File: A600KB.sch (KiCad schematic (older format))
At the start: 84 parts

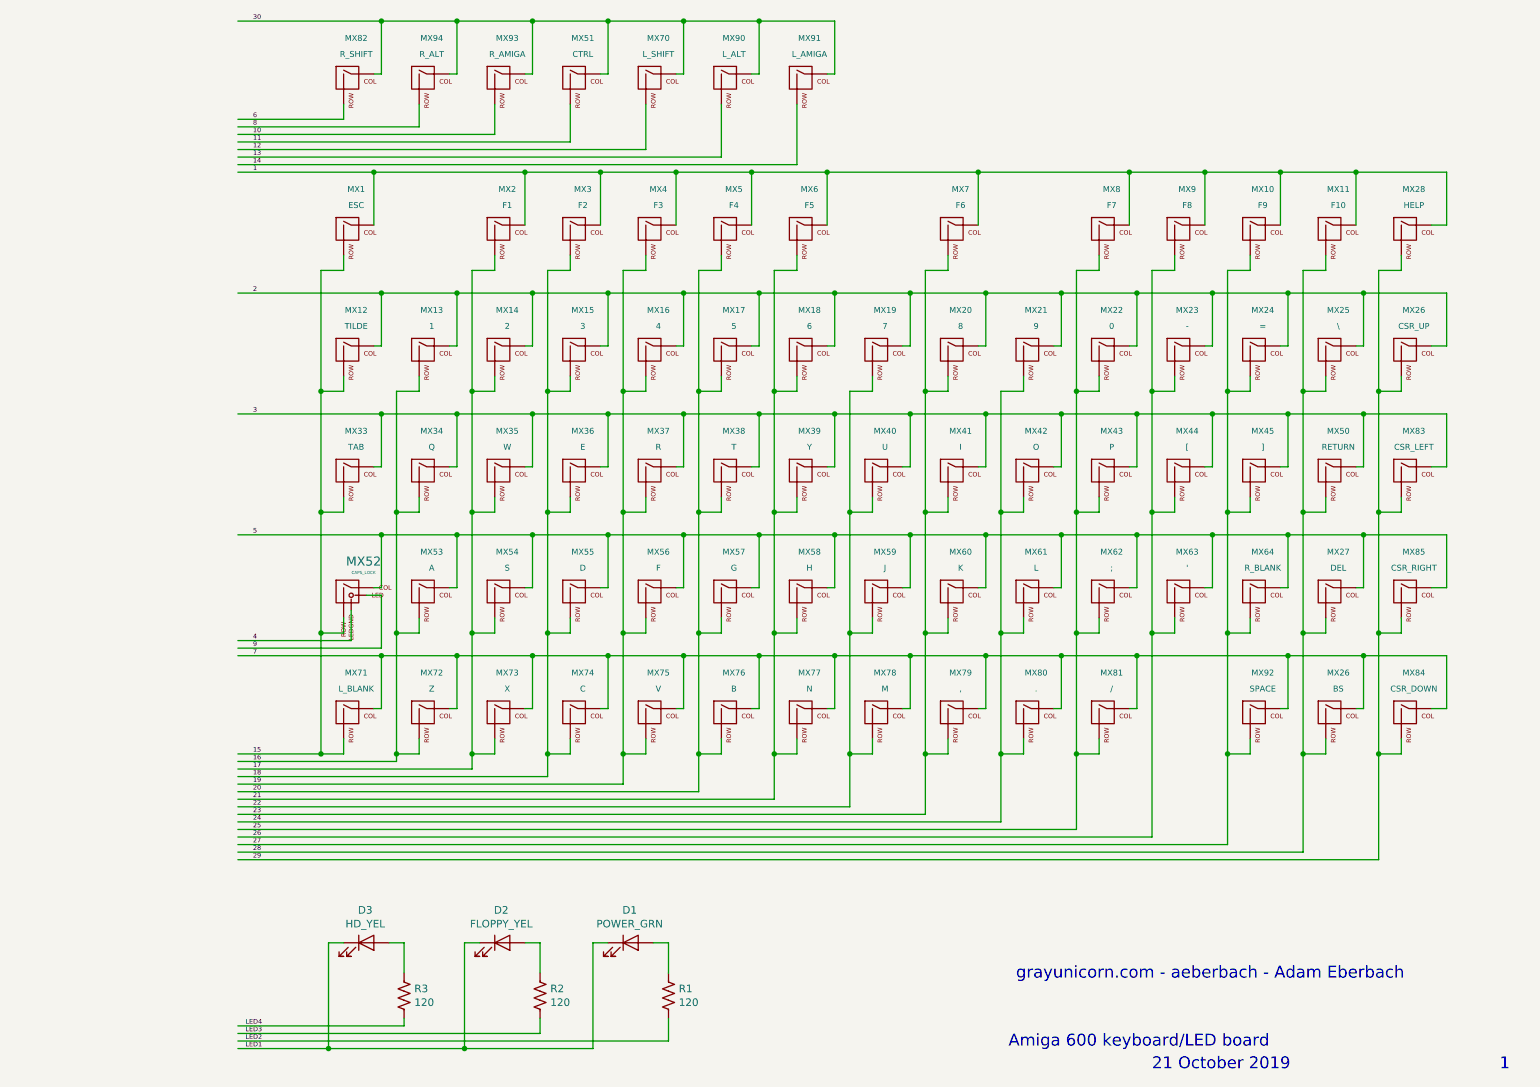
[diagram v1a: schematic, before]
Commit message: footprints for connectors
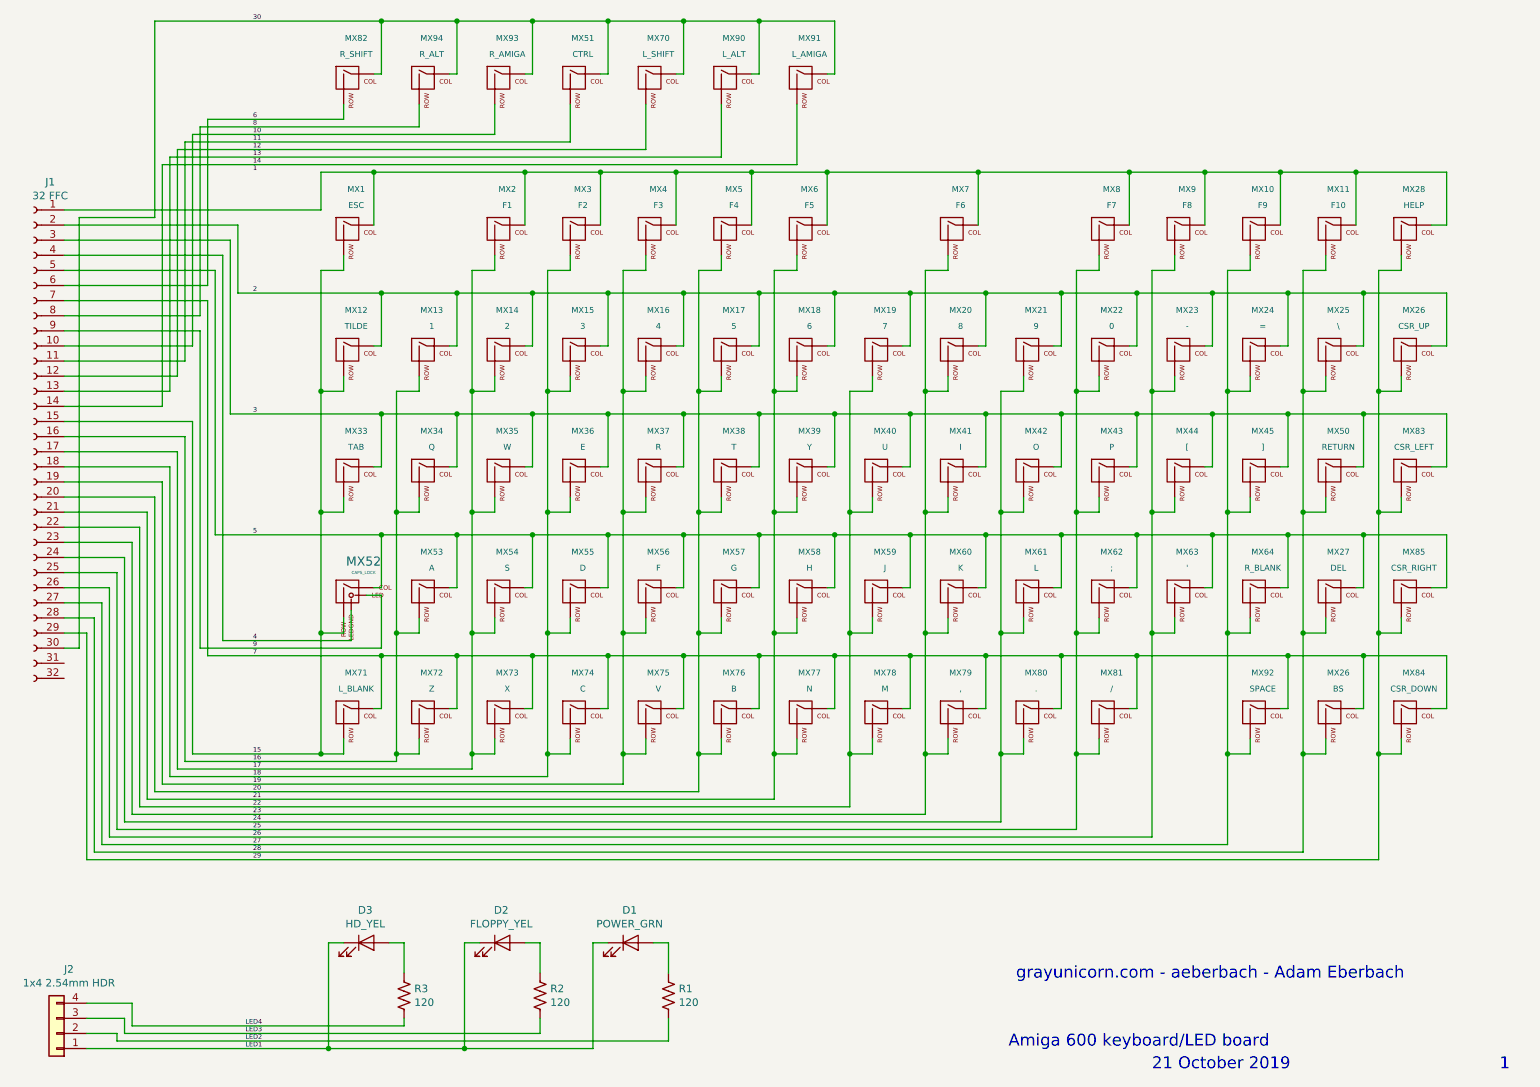
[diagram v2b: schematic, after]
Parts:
- added J1: 32 FFC, A1200KB:FFC-1.25mm-RA-5204403245, symbol Connector:Conn_01x32_Female
- added J2: 1x4 2.54mm HDR, Connector_PinHeader_2.54mm:PinHeader_1x04_P2.54mm_Vertical, symbol Connector_Generic:Conn_01x04
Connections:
- wire segments 490 -> 558
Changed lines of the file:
@@
 	3050 1250 3050 1350
 Wire Wire Line
-	3050 1350 2350 1350
-Wire Wire Line
 	3550 1250 3550 1400
 Wire Wire Line
-	3550 1400 2350 1400
-Wire Wire Line
 	4050 1250 4050 1450
 Wire Wire Line
-	4050 1450 2350 1450
-Wire Wire Line
 	4550 1250 4550 1500
 Wire Wire Line
-	4550 1500 2350 1500
-Wire Wire Line
 	5050 1250 5050 1550
 Wire Wire Line
-	5050 1550 2350 1550
-Wire Wire Line
 	5550 1250 5550 1600
 Wire Wire Line
-	5550 1600 2350 1600
-Wire Wire Line
 	6050 1250 6050 1650
-Wire Wire Line
-	6050 1650 2350 1650
 $Comp
 L MX_Alps_Hybrid:MX-NoLED MX1
@@
 	3900 5550 3900 4750
 Wire Wire Line
-	2350 5700 4400 5700
-Wire Wire Line
 	4400 5700 4400 5550
 Wire Wire Line
 	4400 2350 4550 2350
 Wire Wire Line
-	2350 5750 4900 5750
-Wire Wire Line
 	4900 5750 4900 5550
 Wire Wire Line
 	4900 2350 5050 2350
 Wire Wire Line
-	2350 5800 5400 5800
-Wire Wire Line
 	5400 5800 5400 5550
 Wire Wire Line
 	5400 2350 5550 2350
 Wire Wire Line
-	2350 5850 5900 5850
-Wire Wire Line
 	5900 5850 5900 5550
 Wire Wire Line
 	5900 2350 6050 2350
 Wire Wire Line
-	2350 5900 6400 5900
-Wire Wire Line
 	6400 5900 6400 5550
 Wire Wire Line
 	6400 3150 6550 3150
 Wire Wire Line
-	2350 5950 6900 5950
-Wire Wire Line
 	6900 5950 6900 5550
 Wire Wire Line
 	6900 2350 7050 2350
 Wire Wire Line
-	2350 6000 7400 6000
-Wire Wire Line
 	7400 6000 7400 5550
 Wire Wire Line
@@
 	7900 2350 7900 3150
 Wire Wire Line
-	7900 6050 2350 6050
-Wire Wire Line
-	2350 6100 8400 6100
-Wire Wire Line
 	8400 6100 8400 4750
 Wire Wire Line
@@
 	8900 2350 8900 3150
 Wire Wire Line
-	8900 6150 2350 6150
-Wire Wire Line
-	2350 6200 9400 6200
-Wire Wire Line
 	9400 6200 9400 5550
 Wire Wire Line
@@
 Wire Wire Line
 	9900 2350 9900 3150
-Wire Wire Line
-	9900 6250 2350 6250
 Wire Wire Line
 	10050 5550 9900 5550
@@
 	3050 5450 3050 5550
 Wire Wire Line
-	3900 5650 2350 5650
-Wire Wire Line
 	3400 4750 3400 5550
-Wire Wire Line
-	3400 5600 2350 5600
 Connection ~ 3400 4750
 Wire Wire Line
 	3050 5550 2900 5550
-Wire Wire Line
-	2900 5550 2350 5550
 Connection ~ 2900 5550
 Wire Wire Line
@@
 	3400 5550 3400 5600
 Wire Wire Line
-	2350 1700 3250 1700
-Wire Wire Line
 	9750 2050 9750 1700
 Wire Wire Line
@@
 Wire Wire Line
 	3250 2050 3250 1700
-Connection ~ 3250 1700
 Wire Wire Line
 	3250 1700 4250 1700
-Wire Wire Line
-	2350 4100 3300 4100
 Wire Wire Line
 	10350 4100 10350 4450
@@
 Connection ~ 3300 4900
 Wire Wire Line
-	3300 4900 2350 4900
-Wire Wire Line
 	3750 5250 3800 5250
 Wire Wire Line
@@
 Connection ~ 3300 3300
 Wire Wire Line
-	3300 3300 2350 3300
-Wire Wire Line
 	3750 3650 3800 3650
 Wire Wire Line
@@
 Wire Wire Line
 	3300 2500 3800 2500
-Wire Wire Line
-	2350 700  3300 700
 Wire Wire Line
 	6300 700  6300 1050
@@
 	3300 4500 3300 4850
 Wire Wire Line
-	3300 4850 2350 4850
-Wire Wire Line
 	3100 4600 3100 4800
-Wire Wire Line
-	3100 4800 2350 4800
 Text Label 2450 4850 0    31   ~ 0
 9
@@
 	3450 7300 3450 7350
 Wire Wire Line
-	3450 7350 2350 7350
-Wire Wire Line
 	4350 7300 4350 7400
 Wire Wire Line
-	4350 7400 2350 7400
-Wire Wire Line
 	5200 7300 5200 7450
-Wire Wire Line
-	5200 7450 2350 7450
 Wire Wire Line
 	4800 6800 4700 6800
@@
 	2950 6800 2950 7500
 Connection ~ 2950 7500
-Wire Wire Line
-	2950 7500 2350 7500
 Text Label 2400 7500 0    31   ~ 0
 LED1
@@
 Text Notes 7500 7050 0    79   ~ 0
 grayunicorn.com - aeberbach - Adam Eberbach
+$Comp
+L Connector:Conn_01x32_Female J1
+U 1 1 5EF715D8
+P 1000 3450
+F 0 "J1" H 892 5135 50  0000 C CNN
+F 1 "32 FFC" H 892 5044 50  0000 C CNN
+F 2 "A1200KB:FFC-1.25mm-RA-5204403245" H 1000 3450 50  0001 C CNN
+F 3 "~" H 1000 3450 50  0001 C CNN
+	1    1000 3450
+	-1   0    0    -1
+$EndComp
+$Comp
+L Connector_Generic:Conn_01x04 J2
+U 1 1 5EF8DD47
+P 1150 7400
+F 0 "J2" H 1068 6975 50  0000 C CNN
+F 1 "1x4 2.54mm HDR" H 1068 7066 50  0000 C CNN
+F 2 "Connector_PinHeader_2.54mm:PinHeader_1x04_P2.54mm_Vertical" H 1150 7400 50  0001 C CNN
+F 3 "~" H 1150 7400 50  0001 C CNN
+	1    1150 7400
+	-1   0    0    1
+$EndComp
+Wire Wire Line
+	1350 7500 2950 7500
+Wire Wire Line
+	1550 7450 1550 7400
+Wire Wire Line
+	1550 7400 1350 7400
+Wire Wire Line
+	1550 7450 5200 7450
+Wire Wire Line
+	1600 7400 1600 7300
+Wire Wire Line
+	1600 7300 1350 7300
+Wire Wire Line
+	1600 7400 4350 7400
+Wire Wire Line
+	1650 7350 1650 7200
+Wire Wire Line
+	1650 7200 1350 7200
+Wire Wire Line
+	1650 7350 3450 7350
+Wire Wire Line
+	2350 2500 2350 2050
+Wire Wire Line
+	2350 2050 1200 2050
+Wire Wire Line
+	2300 3300 2300 2150
+Wire Wire Line
+	2300 2150 1200 2150
+Wire Wire Line
+	2300 3300 3300 3300
+Wire Wire Line
+	2250 4800 2250 2250
+Wire Wire Line
+	2250 2250 1200 2250
+Wire Wire Line
+	2250 4800 3100 4800
+Wire Wire Line
+	1200 2350 2200 2350
+Wire Wire Line
+	2200 2350 2200 4100
+Wire Wire Line
+	2200 4100 3300 4100
+Wire Wire Line
+	2150 1350 2150 2450
+Wire Wire Line
+	2150 2450 1200 2450
+Wire Wire Line
+	2150 1350 3050 1350
+Wire Wire Line
+	2150 4900 2150 2550
+Wire Wire Line
+	2150 2550 1200 2550
+Wire Wire Line
+	2150 4900 3300 4900
+Wire Wire Line
+	2100 1400 2100 2650
+Wire Wire Line
+	2100 2650 1200 2650
+Wire Wire Line
+	2100 1400 3550 1400
+Wire Wire Line
+	2100 4850 2100 2750
+Wire Wire Line
+	2100 2750 1200 2750
+Wire Wire Line
+	2100 4850 3300 4850
+Wire Wire Line
+	2050 1450 2050 2850
+Wire Wire Line
+	2050 2850 1200 2850
+Wire Wire Line
+	2050 1450 4050 1450
+Wire Wire Line
+	2000 1500 2000 2950
+Wire Wire Line
+	2000 2950 1200 2950
+Wire Wire Line
+	2000 1500 4550 1500
+Wire Wire Line
+	1950 1550 1950 3050
+Wire Wire Line
+	1950 3050 1200 3050
+Wire Wire Line
+	1950 1550 5050 1550
+Wire Wire Line
+	1900 1600 1900 3150
+Wire Wire Line
+	1900 3150 1200 3150
+Wire Wire Line
+	1900 1600 5550 1600
+Wire Wire Line
+	1850 1650 1850 3250
+Wire Wire Line
+	1850 3250 1200 3250
+Wire Wire Line
+	1850 1650 6050 1650
+Wire Wire Line
+	2050 5550 2050 3350
+Wire Wire Line
+	2050 3350 1200 3350
+Wire Wire Line
+	2050 5550 2900 5550
+Wire Wire Line
+	2000 5600 2000 3450
+Wire Wire Line
+	2000 3450 1200 3450
+Wire Wire Line
+	2000 5600 3400 5600
+Wire Wire Line
+	1950 5650 1950 3550
+Wire Wire Line
+	1950 3550 1200 3550
+Wire Wire Line
+	1950 5650 3900 5650
+Wire Wire Line
+	1900 5700 1900 3650
+Wire Wire Line
+	1900 3650 1200 3650
+Wire Wire Line
+	1900 5700 4400 5700
+Wire Wire Line
+	1850 5750 1850 3750
+Wire Wire Line
+	1850 3750 1200 3750
+Wire Wire Line
+	1850 5750 4900 5750
+Wire Wire Line
+	1800 5800 1800 3850
+Wire Wire Line
+	1800 3850 1200 3850
+Wire Wire Line
+	1800 5800 5400 5800
+Wire Wire Line
+	1750 5850 1750 3950
+Wire Wire Line
+	1750 3950 1200 3950
+Wire Wire Line
+	1750 5850 5900 5850
+Wire Wire Line
+	1700 5900 1700 4050
+Wire Wire Line
+	1700 4050 1200 4050
+Wire Wire Line
+	1700 5900 6400 5900
+Wire Wire Line
+	1650 5950 1650 4150
+Wire Wire Line
+	1650 4150 1200 4150
+Wire Wire Line
+	1650 5950 6900 5950
+Wire Wire Line
+	1600 6000 1600 4250
+Wire Wire Line
+	1600 4250 1200 4250
+Wire Wire Line
+	1600 6000 7400 6000
+Wire Wire Line
+	1550 6050 1550 4350
+Wire Wire Line
+	1550 4350 1200 4350
+Wire Wire Line
+	1550 6050 7900 6050
+Wire Wire Line
+	1500 6100 1500 4450
+Wire Wire Line
+	1500 4450 1200 4450
+Wire Wire Line
+	1500 6100 8400 6100
+Wire Wire Line
+	1450 6150 1450 4550
+Wire Wire Line
+	1450 4550 1200 4550
+Wire Wire Line
+	1450 6150 8900 6150
+Wire Wire Line
+	1400 6200 1400 4650
+Wire Wire Line
+	1400 4650 1200 4650
+Wire Wire Line
+	1400 6200 9400 6200
+Wire Wire Line
+	1350 6250 1350 4750
+Wire Wire Line
+	1350 4750 1200 4750
+Wire Wire Line
+	1350 6250 9900 6250
+Wire Wire Line
+	1200 4850 1300 4850
+Wire Wire Line
+	1300 4850 1300 2000
+Wire Wire Line
+	1300 2000 1800 2000
+Wire Wire Line
+	1800 2000 1800 700
+Wire Wire Line
+	1800 700  3300 700
+Wire Wire Line
+	2900 1950 2900 1700
+Wire Wire Line
+	2900 1700 3250 1700
+Wire Wire Line
+	1200 1950 2900 1950
+Connection ~ 3250 1700
 $EndSCHEMATC

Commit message: correct annotations
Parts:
- renumbered MX26 to MX65
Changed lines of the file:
@@
 	10050 2250 10050 2350
 $Comp
-L MX_Alps_Hybrid:MX-NoLED MX26
+L MX_Alps_Hybrid:MX-NoLED MX65
 U 1 1 5DB06ED2
 P 10100 2900
-F 0 "MX26" H 10133 3187 39  0000 C CNN
+F 0 "MX65" H 10133 3187 39  0000 C CNN
 F 1 "CSR_UP" H 10133 3081 39  0000 C CNN
 F 2 "MX_Only:MXOnly-1U-NoLED" H 9475 2875 60  0001 C CNN

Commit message: Finished, sent to fab
PCB Order
Weight:
1kg
Project Name:
A600 r1
Length:
325
Width:
125
Total Quantity:
6
Layers:
Two Layer
PCB Thickness:
3.2 mm
Material Type:
FR 4
Copper Weight:
1 oz
Surface Finish:
HASL
Solder Mask Color:
Green
Silk Screen Color:
White
Smallest Hole:
0.10 mm
Min Trace/Space:
0.20 mm
Express Options:
Optional
Tooling:
52.5
PCB Total:
48.78046875
Ship Weight:
0.9750000000000001
Lead Time (Manufacturing):
5 Days
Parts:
- MX33: footprint MX_Only:MXOnly-2.25U-NoLED -> MX_Only:MXOnly-2U-NoLED
- MX70, MX82: footprint MX_Only:MXOnly-2U-NoLED -> MX_Only:MXOnly-1.75U-NoLED
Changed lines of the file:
@@
 F 0 "MX82" H 3133 1387 39  0000 C CNN
 F 1 "R_SHIFT" H 3133 1281 39  0000 C CNN
-F 2 "MX_Only:MXOnly-2U-NoLED" H 2475 1075 60  0001 C CNN
+F 2 "MX_Only:MXOnly-1.75U-NoLED" H 2475 1075 60  0001 C CNN
 F 3 "" H 2475 1075 60  0001 C CNN
 	1    3100 1100
@@
 F 0 "MX70" H 5133 1387 39  0000 C CNN
 F 1 "L_SHIFT" H 5133 1281 39  0000 C CNN
-F 2 "MX_Only:MXOnly-2U-NoLED" H 4475 1075 60  0001 C CNN
+F 2 "MX_Only:MXOnly-1.75U-NoLED" H 4475 1075 60  0001 C CNN
 F 3 "" H 4475 1075 60  0001 C CNN
 	1    5100 1100
@@
 F 0 "MX33" H 3133 3987 39  0000 C CNN
 F 1 "TAB" H 3133 3881 39  0000 C CNN
-F 2 "MX_Only:MXOnly-2.25U-NoLED" H 2475 3675 60  0001 C CNN
+F 2 "MX_Only:MXOnly-2U-NoLED" H 2475 3675 60  0001 C CNN
 F 3 "" H 2475 3675 60  0001 C CNN
 	1    3100 3700
